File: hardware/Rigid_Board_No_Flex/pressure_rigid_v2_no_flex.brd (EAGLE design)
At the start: 106.9 x 71.6 mm, 44 parts, among them M1 ARDUINO_R3_ICSP_NODIM

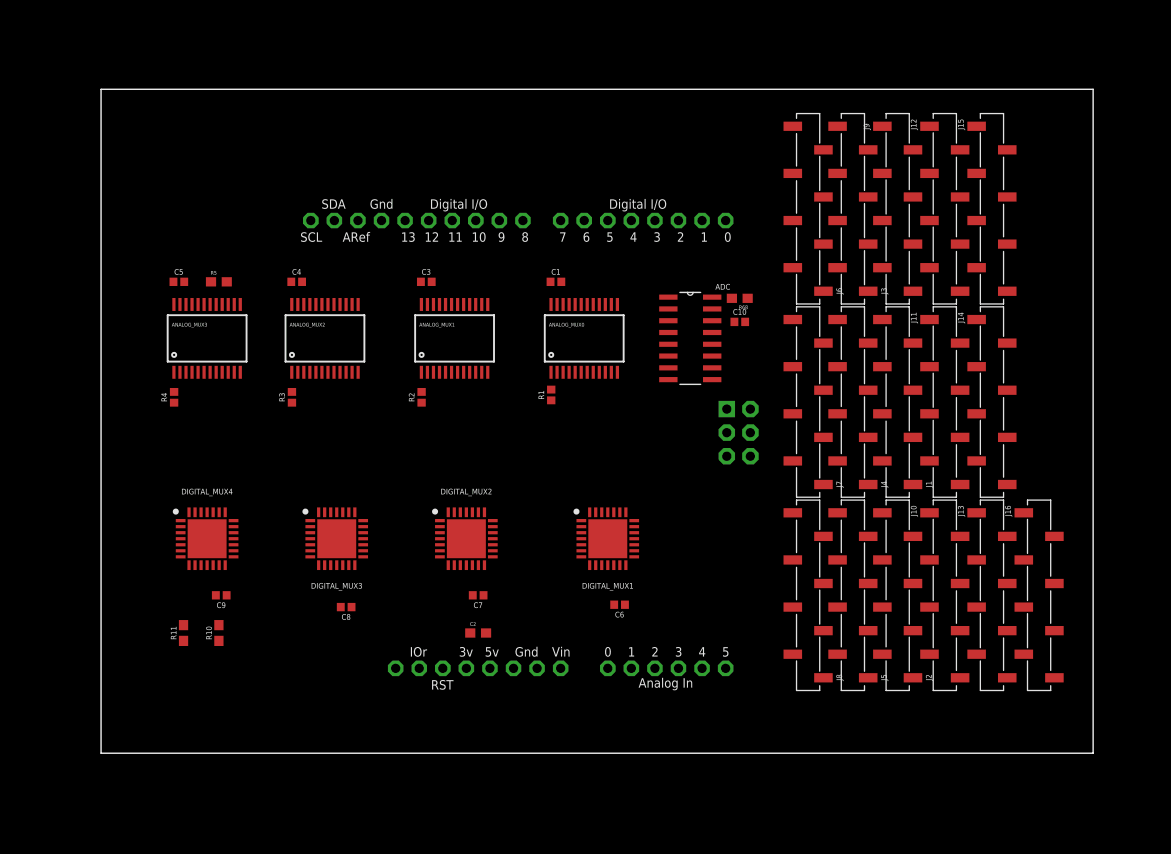
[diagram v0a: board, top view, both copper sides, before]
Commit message: Removed flex pin connectors
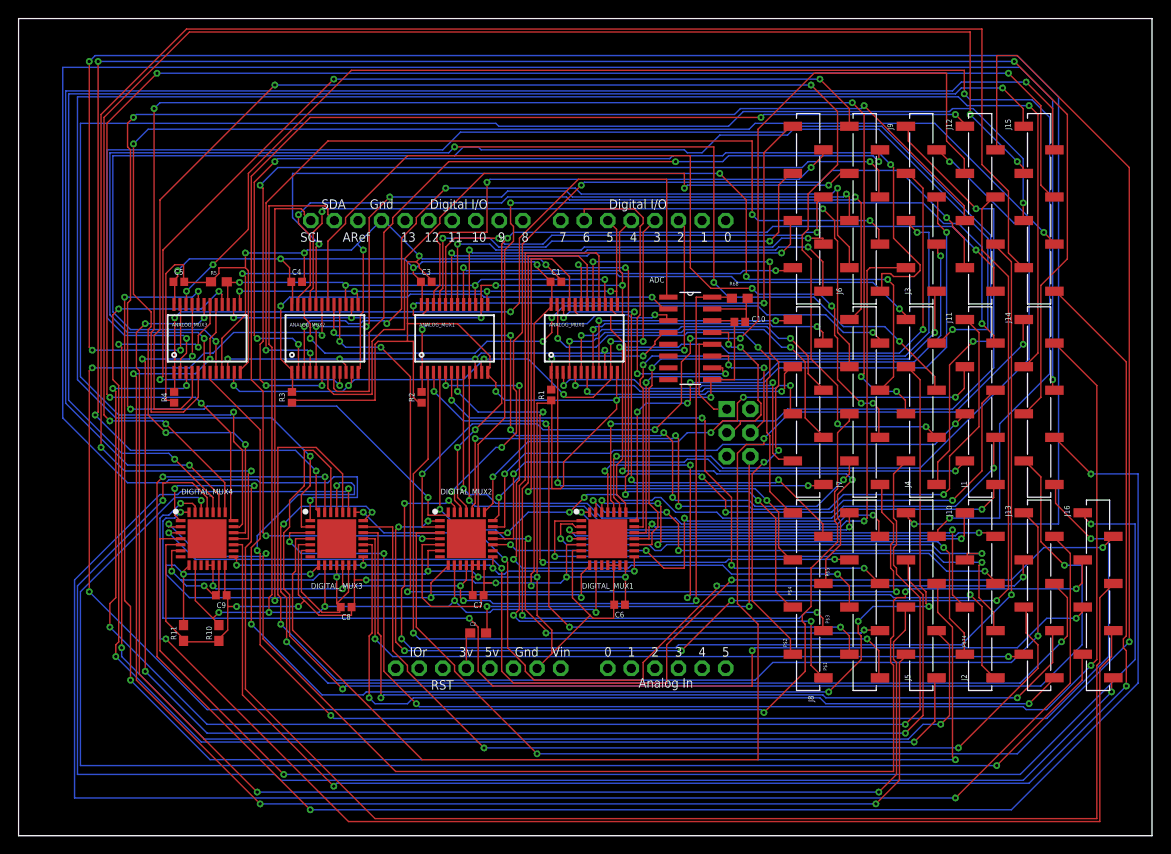
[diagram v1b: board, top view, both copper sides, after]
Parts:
- moved J16 6.35 mm to (103.6, 19.3)
- moved J13 5.08 mm to (97.3, 19.3)
- moved J14 5.08 mm to (97.3, 40.1)
- moved J15 5.08 mm to (97.3, 61.0)
- moved J10 3.81 mm to (90.9, 19.3)
- moved J11 3.81 mm to (90.9, 40.1)
- moved J12 3.81 mm to (90.9, 61.0)
- moved J1 2.54 mm to (84.6, 22.4)
- moved J2 2.54 mm to (84.6, 1.52)
- moved J9 2.54 mm to (84.6, 61.0)
- moved J3 1.27 mm to (78.5, 43.2)
- moved J4 1.27 mm to (78.5, 22.4)
- moved J5 1.27 mm to (78.5, 1.52)
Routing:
- net GND: track 0.00 -> 348.8 mm, vias 0 -> 14
- net P$109: track 0.00 -> 222.2 mm, vias 0 -> 2
- net P$56: track 0.00 -> 215.4 mm, vias 0 -> 4
- net P$108: track 0.00 -> 210.2 mm, vias 0 -> 4
- net 3.3V0: track 0.00 -> 202.8 mm, vias 0 -> 11
- net P$110: track 0.00 -> 200.1 mm, vias 0 -> 2
- net P$107: track 0.00 -> 192.3 mm, vias 0 -> 4
- net P$103: track 0.00 -> 188.6 mm, vias 0 -> 2
- net P$114: track 0.00 -> 188.5 mm, vias 0 -> 2
- net P$95: track 0.00 -> 181.3 mm, vias 0 -> 2
- net P$116: track 0.00 -> 170.7 mm, vias 0 -> 2
- net P$92: track 0.00 -> 169.0 mm, vias 0 -> 4
- net P$117: track 0.00 -> 169.0 mm, vias 0 -> 4
- net P$119: track 0.00 -> 168.8 mm, vias 0 -> 2
- net P$36: track 0.00 -> 168.7 mm, vias 0 -> 4
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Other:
- board size 106.9 x 71.6 mm -> 122.2 x 88.1 mm
- board text added: "P$1"
- board text added: "P$2"
- board text added: "P$3"
- board text added: "P$4"
- board text added: "P$5"
- board text added: "P$74"
